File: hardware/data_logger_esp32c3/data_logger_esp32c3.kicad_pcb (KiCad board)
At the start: 2 copper layers, 5 parts, among them U1 ESP32-C3-MINI-1

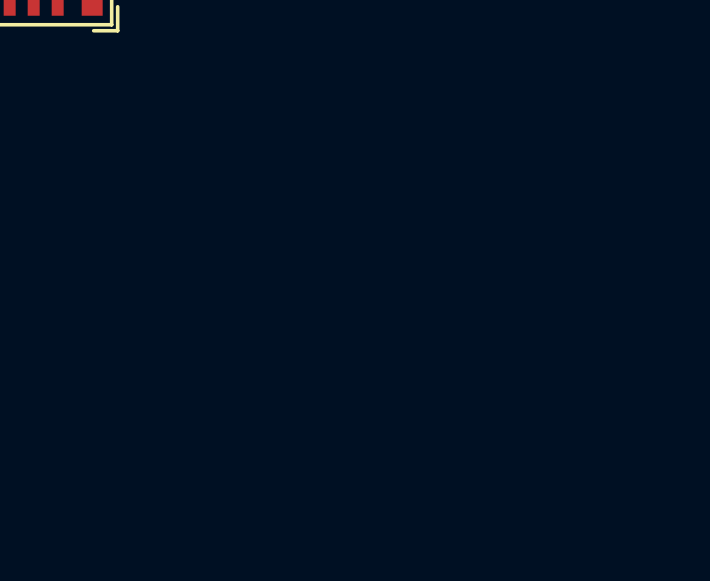
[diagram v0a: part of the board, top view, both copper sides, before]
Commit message: add connector
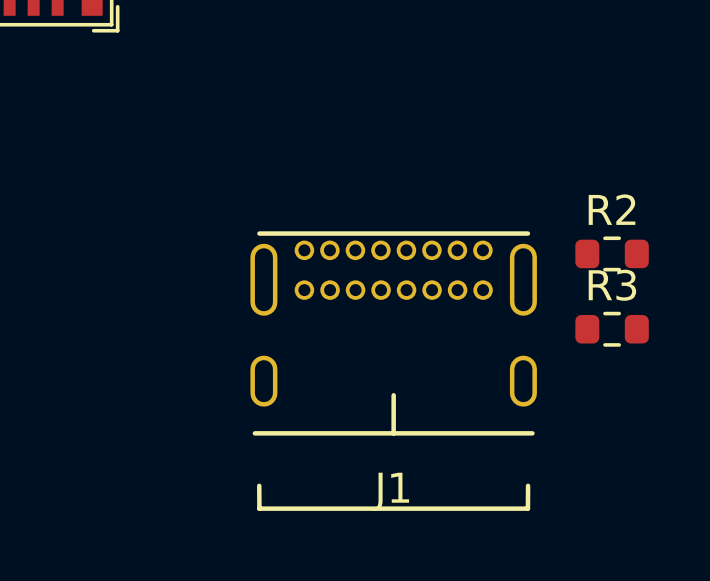
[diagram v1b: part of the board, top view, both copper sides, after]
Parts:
- added J1: USB_C_Receptacle_USB2.0, type_c:USB_C_GCT_USB4085, F.Cu at (134.6, 99.1)
- added R2: 5.1k, Resistor_SMD:R_0603_1608Metric, F.Cu at (141.9, 93.1)
- added R3: 5.1k, Resistor_SMD:R_0603_1608Metric, F.Cu at (141.9, 95.6)
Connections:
- U1 pad 26: unconnected-(U1-Pad26) -> D-
- U1 pad 27: unconnected-(U1-Pad27) -> D+

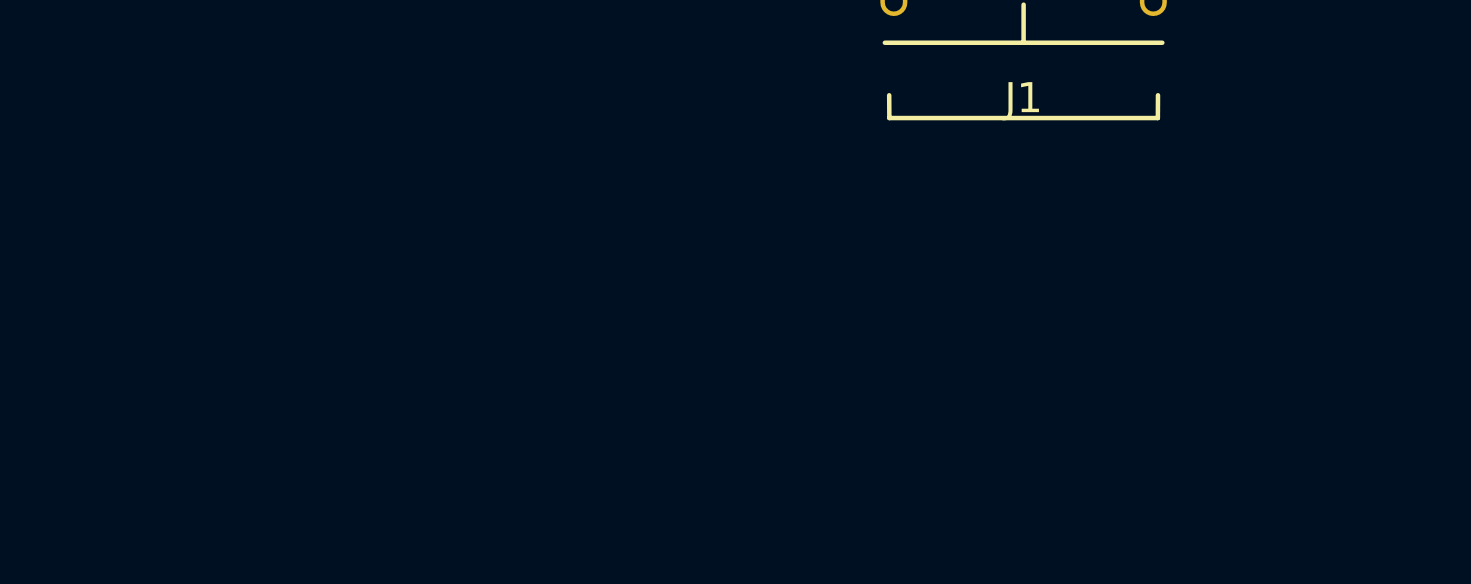
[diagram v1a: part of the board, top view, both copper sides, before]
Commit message: Added regulator circuit
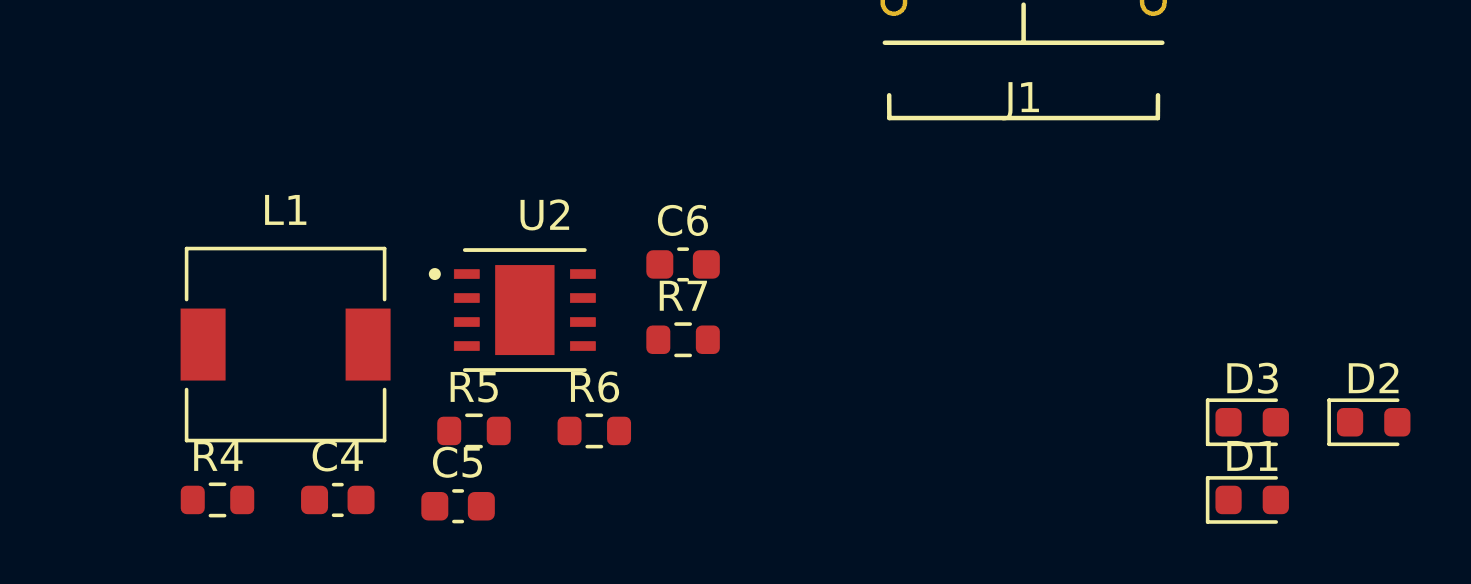
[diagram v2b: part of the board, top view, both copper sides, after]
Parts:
- added C4: 100uF, Capacitor_SMD:C_0603_1608Metric, F.Cu at (111.8, 114.3)
- added C5: 470pF, Capacitor_SMD:C_0603_1608Metric, F.Cu at (115.8, 114.5)
- added C6: 470uF, Capacitor_SMD:C_0603_1608Metric, F.Cu at (123.3, 106.5)
- added D1: D_Zener_Small_Filled, Diode_SMD:D_0603_1608Metric, F.Cu at (142.2, 114.3)
- added D2: D_Zener_Small_Filled, Diode_SMD:D_0603_1608Metric, F.Cu at (146.3, 111.7)
- added D3: D_Zener_Small_Filled, Diode_SMD:D_0603_1608Metric, F.Cu at (142.2, 111.7)
- added L1: 220uH, Inductor_SMD:L_6.3x6.3_H3, F.Cu at (110.0, 109.1)
- added R4: 10k, Resistor_SMD:R_0603_1608Metric, F.Cu at (107.8, 114.3)
- added R5: 0.33, Resistor_SMD:R_0603_1608Metric, F.Cu at (116.3, 112.0)
- added R6: 2k, Resistor_SMD:R_0603_1608Metric, F.Cu at (120.3, 112.0)
- added R7: 3.28k, Resistor_SMD:R_0603_1608Metric, F.Cu at (123.3, 109.0)
- added U2: MC34063ADRJR, lib:8-WDFN Exposed Pad, F.Cu at (118.0, 108.0)
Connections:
- net VBUS renamed +5V

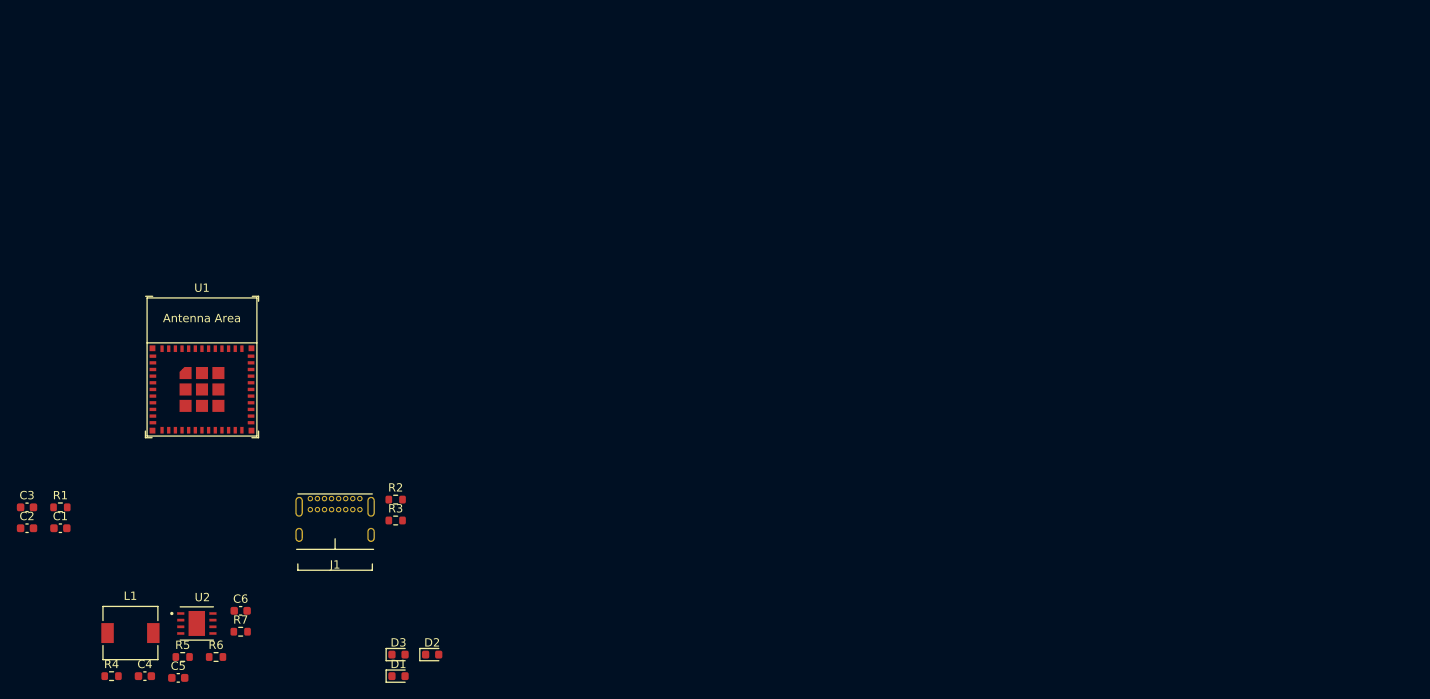
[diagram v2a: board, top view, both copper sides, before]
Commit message: Added uSD circuit
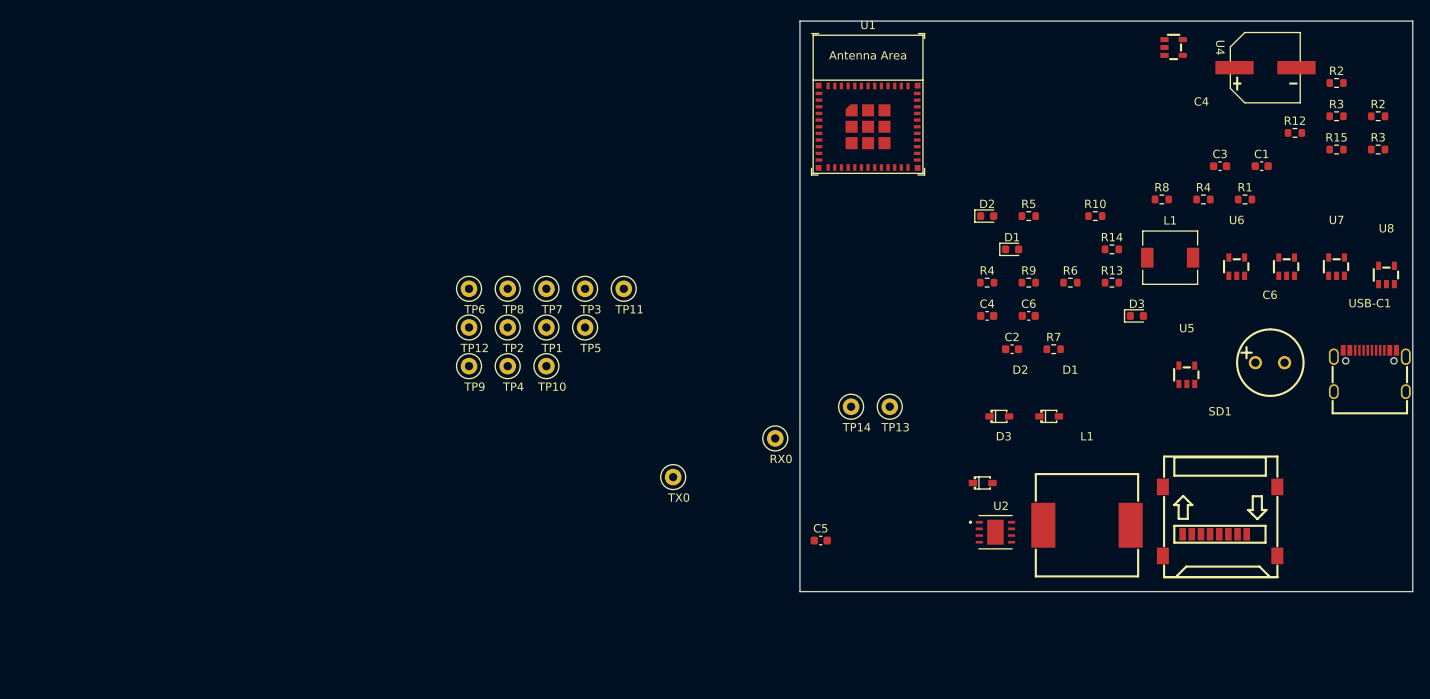
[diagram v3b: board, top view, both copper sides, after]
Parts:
- removed J1: USB_C_Receptacle_USB2.0, type_c:USB_C_GCT_USB4085
- added C4: 100uF, lib:RT1H101M0810, F.Cu at (249.0, 31.0)
- added C6: KF471M016F115A, lib:KF471M016F115A, F.Cu at (247.0, 69.0)
- added D1: B0530WS_SE, lib:B0530WS_SE, F.Cu at (223.0, 78.0)
- added D2: B0530WS_SE, lib:B0530WS_SE, F.Cu at (217.0, 78.0)
- added D3: B0530WS_SE, lib:B0530WS_SE, F.Cu at (215.0, 86.0)
- added L1: 220uH, lib:SMDRI127-221MT, F.Cu at (225.0, 86.0)
- added R10: 1.6k, Resistor_SMD:R_0603_1608Metric, F.Cu at (226.0, 59.0)
- added R12: 7.5k, Resistor_SMD:R_0603_1608Metric, F.Cu at (250.0, 49.0)
- added R13: 1k, Resistor_SMD:R_0603_1608Metric, F.Cu at (228.0, 67.0)
- added R14: 1k, Resistor_SMD:R_0603_1608Metric, F.Cu at (228.0, 63.0)
- added R15: 1k, Resistor_SMD:R_0603_1608Metric, F.Cu at (255.0, 51.0)
- added R2: 5.1k, Resistor_SMD:R_0603_1608Metric, F.Cu at (260.0, 47.0)
- added R3: 5.1k, Resistor_SMD:R_0603_1608Metric, F.Cu at (255.0, 47.0)
- added R4: 10k, Resistor_SMD:R_0603_1608Metric, F.Cu at (239.0, 57.0)
- added R8: 10k, Resistor_SMD:R_0603_1608Metric, F.Cu at (234.0, 57.0)
- added R9: 10k, Resistor_SMD:R_0603_1608Metric, F.Cu at (218.0, 67.0)
- added RX0: TestPoint, TestPoint:TestPoint_Loop_D2.50mm_Drill1.0mm, F.Cu at (187.5, 85.7)
- added SD1: 472192001, lib:472192001, F.Cu at (241.0, 83.0)
- added TP1: TestPoint, TestPoint:TestPoint_Loop_D2.50mm_Drill1.0mm, F.Cu at (160.0, 72.4)
- added TP10: TestPoint, TestPoint:TestPoint_Loop_D2.50mm_Drill1.0mm, F.Cu at (160.0, 77.0)
- added TP11: TestPoint, TestPoint:TestPoint_Loop_D2.50mm_Drill1.0mm, F.Cu at (169.3, 67.7)
- added TP12: TestPoint, TestPoint:TestPoint_Loop_D2.50mm_Drill1.0mm, F.Cu at (150.7, 72.4)
- added TP13: TestPoint, TestPoint:TestPoint_Loop_D2.50mm_Drill1.0mm, F.Cu at (201.3, 81.9)
- added TP14: TestPoint, TestPoint:TestPoint_Loop_D2.50mm_Drill1.0mm, F.Cu at (196.6, 81.9)
- added TP2: TestPoint, TestPoint:TestPoint_Loop_D2.50mm_Drill1.0mm, F.Cu at (155.4, 72.4)
- added TP3: TestPoint, TestPoint:TestPoint_Loop_D2.50mm_Drill1.0mm, F.Cu at (164.7, 67.7)
- added TP4: TestPoint, TestPoint:TestPoint_Loop_D2.50mm_Drill1.0mm, F.Cu at (155.4, 77.0)
- added TP5: TestPoint, TestPoint:TestPoint_Loop_D2.50mm_Drill1.0mm, F.Cu at (164.7, 72.4)
- added TP6: TestPoint, TestPoint:TestPoint_Loop_D2.50mm_Drill1.0mm, F.Cu at (150.7, 67.7)
- added TP7: TestPoint, TestPoint:TestPoint_Loop_D2.50mm_Drill1.0mm, F.Cu at (160.0, 67.7)
- added TP8: TestPoint, TestPoint:TestPoint_Loop_D2.50mm_Drill1.0mm, F.Cu at (155.4, 67.7)
- added TP9: TestPoint, TestPoint:TestPoint_Loop_D2.50mm_Drill1.0mm, F.Cu at (150.7, 77.0)
- added TX0: TestPoint, TestPoint:TestPoint_Loop_D2.50mm_Drill1.0mm, F.Cu at (175.3, 90.4)
- added U3: LM321MF, lib:LM321MF, F.Cu at (249.0, 60.0)
- added U4: LM321MF, lib:LM321MF, F.Cu at (240.5, 38.7)
- added U5: LM321MF, lib:LM321MF, F.Cu at (237.0, 73.0)
- added U6: LM321MF, lib:LM321MF, F.Cu at (243.0, 60.0)
- added U7: LM321MF, lib:LM321MF, F.Cu at (255.0, 60.0)
- added U8: LM321MF, lib:LM321MF, F.Cu at (261.0, 61.0)
- added USB-C1: USB-TYPE-C-018, lib:USB-TYPE-C-018, F.Cu at (259.0, 70.0)
- R6: value 2k -> 1.96k
- R7: value 3.28k -> 3.3k
- moved C1 150.8 mm to (246.0, 53.0)
- moved C3 149.2 mm to (241.0, 53.0)
- moved R1 147.1 mm to (244.0, 57.0)
- moved L1 132.9 mm to (235.0, 64.0)
- moved R3 126.2 mm to (260.0, 51.0)
- moved R2 123.7 mm to (255.0, 43.0)
- moved C2 120.3 mm to (216.0, 75.0)
- moved R4 115.4 mm to (213.0, 67.0)
- moved R5 114.7 mm to (218.0, 59.0)
- moved R6 112.1 mm to (223.0, 67.0)
- moved C4 110.1 mm to (213.0, 71.0)
- moved R7 103.5 mm to (221.0, 75.0)
- moved C6 101.1 mm to (218.0, 71.0)
- moved D3 97.7 mm to (231.0, 71.0)
- moved U2 96.6 mm to (214.0, 97.0)
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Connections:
- C4 pad 1: Net-(C4-Pad1) -> VIN
- D1 pad 1: unconnected-(D1-Pad1) -> VIN
- D2 pad 1: unconnected-(D2-Pad1) -> VIN
- R4 pad 2: Net-(C4-Pad1) -> VIN
- R5 pad 2: Net-(C4-Pad1) -> Net-(D1-Pad1)
- U1 pad 12: unconnected-(U1-Pad12) -> ADC1_CH0
- U1 pad 13: unconnected-(U1-Pad13) -> ADC1_CH1
- U1 pad 18: unconnected-(U1-Pad18) -> ADC1_CH4
- U1 pad 19: unconnected-(U1-Pad19) -> I2S
- U1 pad 20: unconnected-(U1-Pad20) -> CS
- U1 pad 21: unconnected-(U1-Pad21) -> DI
- U1 pad 22: unconnected-(U1-Pad22) -> SCLK
- U1 pad 23: unconnected-(U1-Pad23) -> DO
- U1 pad 30: unconnected-(U1-Pad30) -> Net-(RX0-Pad1)
- U1 pad 31: unconnected-(U1-Pad31) -> Net-(TX0-Pad1)
- U1 pad 5: unconnected-(U1-Pad5) -> ADC1_CH2
- U1 pad 6: unconnected-(U1-Pad6) -> ADC1_CH3
- U2 pad 2: Net-(D3-Pad1) -> Net-(L1-Pad1)
- U2 pad 6: Net-(C4-Pad1) -> Net-(D1-Pad1)
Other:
- board outline added: 73.7 x 68.6 mm

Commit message: laying out board
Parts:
- TP13: moved to B.Cu
- moved C6 59.3 mm to (189.1, 82.2), turned to 90 degrees
- moved USB-C1 37.6 mm to (227.8, 91.1)
- moved TP14 30.7 mm to (220.1, 101.6)
- moved L1 29.6 mm to (201.5, 104.1), turned to 180 degrees
- moved TP13 24.5 mm to (215.7, 101.8), turned to 180 degrees
- moved C5 17.0 mm to (210.0, 98.5), turned to -90 degrees
- moved D2 16.5 mm to (222.3, 93.7)
- moved D1 13.1 mm to (222.5, 91.1)
- moved D3 1.98 mm to (213.1, 86.7)
- moved SD1 1.48 mm to (241.7, 84.3)

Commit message: last commit of the night
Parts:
- removed the L1 at (235.0, 64.0)
- moved C4 65.2 mm to (222.8, 90.8), turned to -90 degrees
- moved U5 55.1 mm to (187.9, 48.1), turned to -90 degrees
- moved SD1 28.9 mm to (212.8, 86.1), turned to 90 degrees
- moved U1 16.0 mm to (201.2, 61.3)
- moved C6 15.1 mm to (203.7, 78.1), turned to 0 degrees
- moved D3 11.0 mm to (212.7, 97.6)
- moved L1 3.24 mm to (201.2, 107.3)
- moved C5 2.12 mm to (210.6, 100.6), turned to 0 degrees
- moved D1 2.06 mm to (220.5, 91.0)
- moved D2 1.86 mm to (220.5, 93.1)
- moved USB-C1 1.55 mm to (226.3, 91.1)
- moved TP14 1.35 mm to (218.8, 101.6)
- moved U2 1.32 mm to (212.7, 97.1)
- moved TP13 1.30 mm to (214.4, 101.7)
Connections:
- C4 pad 1: unconnected-(C4-Pad1) -> GND
- C4 pad 2: unconnected-(C4-Pad2) -> Net-(D1-Pad1)
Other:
- board size 73.7 x 68.6 mm -> 39.2 x 51.4 mm
